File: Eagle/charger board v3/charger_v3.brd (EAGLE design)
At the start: 98.7 x 90.2 mm, 37 parts, among them IC1 IR2110D, Q2 IRFP240, Q3 MJE13003G

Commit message: benerin opto
benerin opto
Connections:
- removed net N$11: OK1.4, R1.2
- new net N$9: OK1.1, R1.2
- net 5V: now also OK1.4; no longer R1.1
- net PWM_SW1: now also R1.1; no longer OK1.1
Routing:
- net N$11: track 12.6 -> 0.00 mm
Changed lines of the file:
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@@
 <?xml version="1.0" encoding="utf-8"?>
 <!DOCTYPE eagle SYSTEM "eagle.dtd">
-<eagle version="9.6.1">
+<eagle version="9.6.2">
 <drawing>
 <settings>
-<setting alwaysvectorfont="yes"/>
+<setting alwaysvectorfont="no"/>
 <setting verticaltext="up"/>
 </settings>
@@
 <contactref element="ESP" pad="2"/>
 <contactref element="LM35" pad="3"/>
-<contactref element="R1" pad="1"/>
 <wire x1="93.98" y1="77.47" x2="93.98" y2="74.93" width="0.3048" layer="1"/>
 <wire x1="82.6008" y1="50.5968" x2="82.6008" y2="54.5592" width="0.3048" layer="16"/>
@@
 <wire x1="92.71" y1="33.02" x2="91.44" y2="33.02" width="0.3048" layer="16"/>
 <wire x1="91.44" y1="33.02" x2="89.5604" y2="34.8996" width="0.3048" layer="16"/>
-<wire x1="82.6008" y1="54.5592" x2="82.55" y2="54.61" width="0.3048" layer="16"/>
 <wire x1="97.282" y1="71.5772" x2="94.0308" y2="74.8284" width="0.3048" layer="16"/>
 <wire x1="97.282" y1="60.2996" x2="97.282" y2="71.5772" width="0.3048" layer="16"/>
@@
 <wire x1="82.6008" y1="54.7116" x2="83.6676" y2="55.7784" width="0.3048" layer="16"/>
 <wire x1="94.0308" y1="74.8284" x2="93.98" y2="74.93" width="0.3048" layer="16"/>
-<wire x1="82.6008" y1="54.7116" x2="82.55" y2="54.61" width="0.3048" layer="16"/>
 <wire x1="85.09" y1="77.47" x2="85.09" y2="78.74" width="0.3048" layer="1"/>
 <wire x1="85.09" y1="78.74" x2="86.36" y2="80.01" width="0.3048" layer="1"/>
@@
 <wire x1="91.44" y1="80.01" x2="93.98" y2="77.47" width="0.3048" layer="1"/>
 <contactref element="IC1" pad="9"/>
+<contactref element="OK1" pad="4"/>
+<wire x1="93.98" y1="74.93" x2="88.9" y2="71.12" width="0" layer="19" extent="1-1"/>
+<wire x1="82.6008" y1="54.5592" x2="82.6008" y2="54.7116" width="0" layer="19" extent="16-16"/>
 </signal>
 <signal name="VB">
@@
 <contactref element="ESP" pad="3"/>
 <contactref element="P_3V3" pad="1"/>
-<contactref element="OK1" pad="1"/>
 <wire x1="81.3816" y1="73.8124" x2="81.3816" y2="71.1708" width="0.3048" layer="16"/>
 <wire x1="82.55" y1="77.47" x2="82.55" y2="74.9808" width="0.3048" layer="16"/>
 <wire x1="82.55" y1="74.9808" x2="81.3816" y2="73.8124" width="0.3048" layer="16"/>
-<wire x1="81.3816" y1="71.1708" x2="81.28" y2="71.12" width="0.3048" layer="16"/>
 <wire x1="90.4748" y1="62.23" x2="92.71" y2="62.23" width="0.3048" layer="16"/>
 <wire x1="81.534" y1="71.1708" x2="90.4748" y2="62.23" width="0.3048" layer="16"/>
-<wire x1="81.534" y1="71.1708" x2="81.28" y2="71.12" width="0.3048" layer="16"/>
+<contactref element="R1" pad="1"/>
+<wire x1="81.534" y1="71.1708" x2="81.3816" y2="71.1708" width="0" layer="19" extent="16-16"/>
+<wire x1="82.55" y1="54.61" x2="92.71" y2="62.23" width="0" layer="19" extent="1-1"/>
 </signal>
 <signal name="PWM_SW2">
@@
 <contactref element="R9" pad="2"/>
 </signal>
-<signal name="N$11">
-<contactref element="OK1" pad="4"/>
+<signal name="N$9">
+<contactref element="OK1" pad="1"/>
 <contactref element="R1" pad="2"/>
-<wire x1="82.6008" y1="62.3316" x2="82.6008" y2="66.7258" width="0.3048" layer="1"/>
-<wire x1="86.995" y1="71.12" x2="88.9" y2="71.12" width="0.3048" layer="1"/>
-<wire x1="82.6008" y1="62.3316" x2="82.55" y2="62.23" width="0.3048" layer="1"/>
-<wire x1="82.6008" y1="66.7258" x2="86.995" y2="71.12" width="0.3048" layer="1"/>
+<wire x1="82.55" y1="62.23" x2="81.28" y2="71.12" width="0" layer="19" extent="1-1"/>
 </signal>
 </signals>

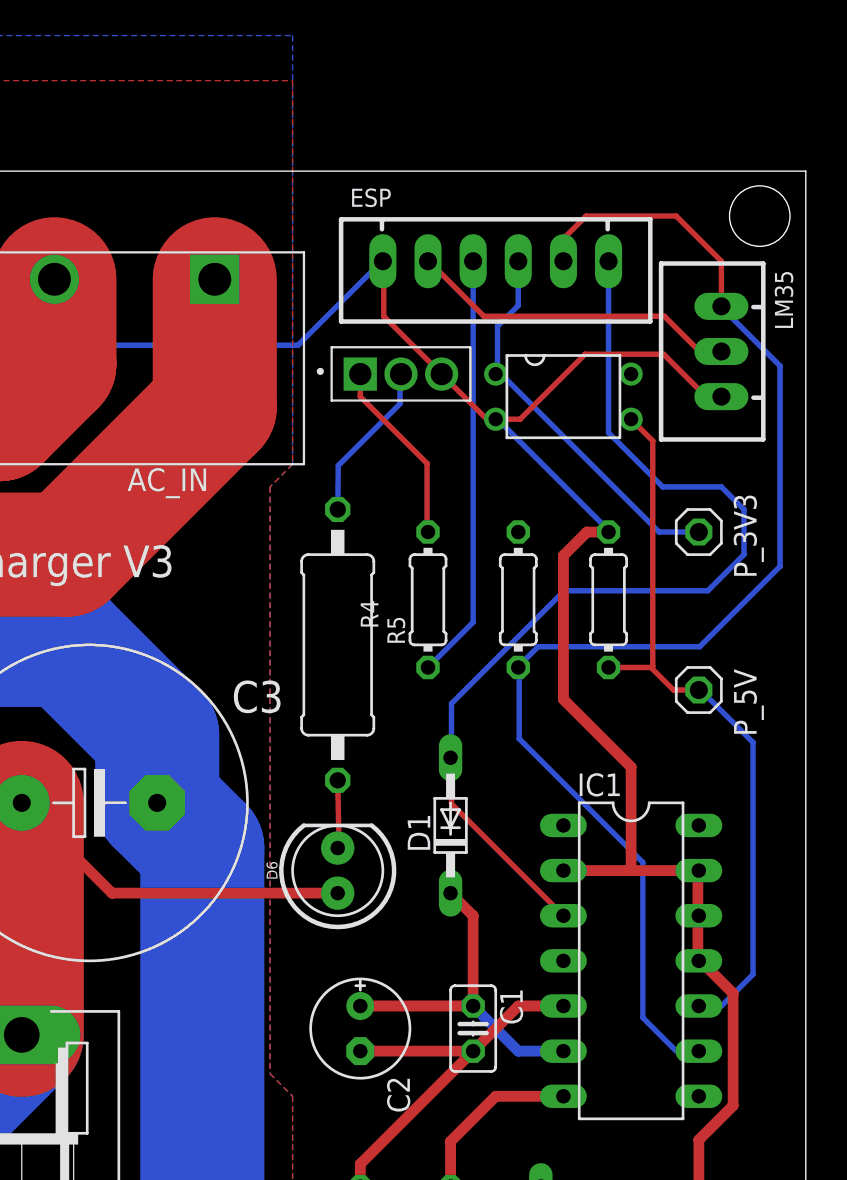
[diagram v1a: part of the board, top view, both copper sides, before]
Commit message: reroute opto
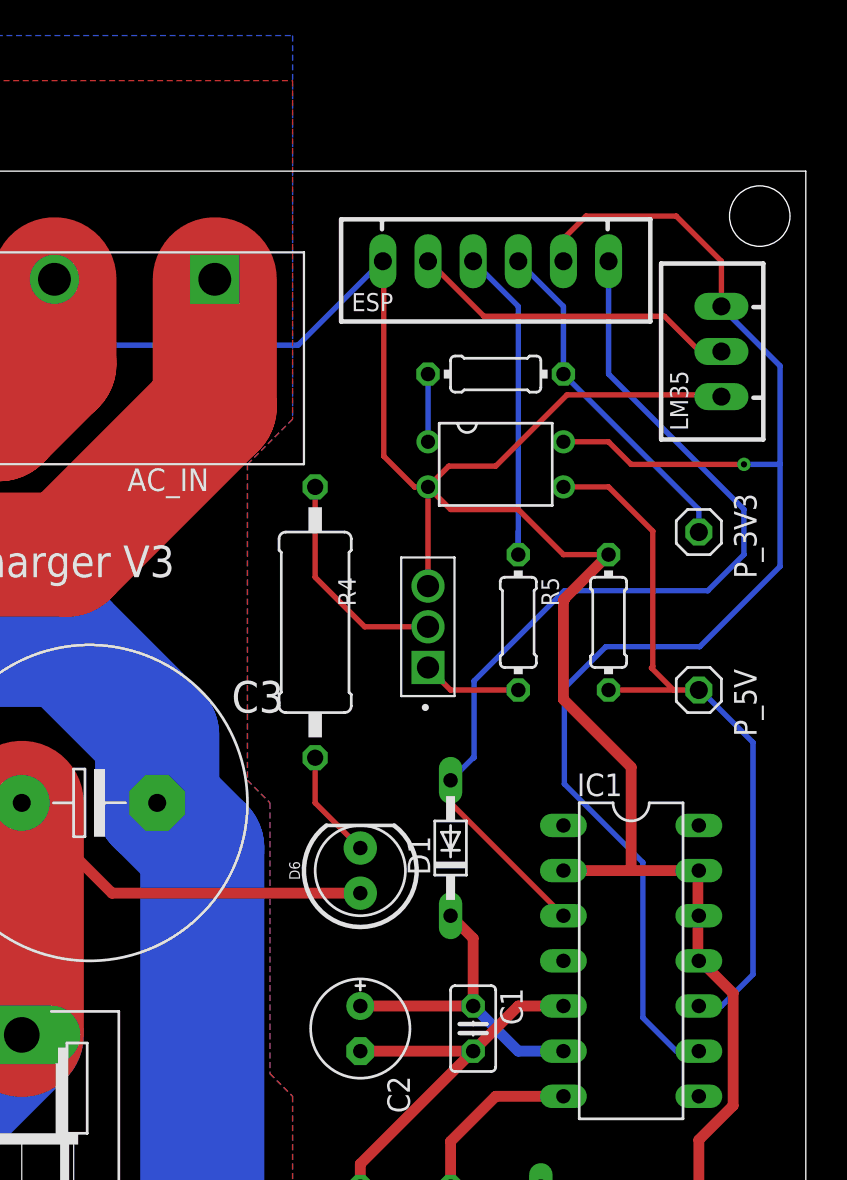
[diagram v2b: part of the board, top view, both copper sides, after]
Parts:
- moved Q3 16.9 mm to (77.5, 54.6), turned to 90 degrees
- moved R1 12.8 mm to (81.3, 71.1), turned to 180 degrees
- moved OK1 5.39 mm to (81.3, 66.0)
- moved R5 5.24 mm to (82.5, 57.1), turned to 270 degrees
- moved R4 1.80 mm to (71.1, 57.1)
- moved R7 1.27 mm to (87.6, 57.1)
- moved D1 1.27 mm to (78.7, 44.5)
- moved D6 1.27 mm to (73.7, 43.2)
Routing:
- net GND: track 345.4 -> 357.6 mm
- net 5V: track 73.7 -> 82.3 mm, vias 0 -> 1
- net PWM_SW2: track 23.9 -> 18.8 mm
- net N$5: track 10.5 -> 5.68 mm
- net N$9: track 0.00 -> 3.81 mm
- net N$3: track 9.07 -> 12.6 mm
- net N$4: track 3.89 -> 6.21 mm
- net PWM_SW1: track 21.7 -> 19.4 mm
- net 12V: track 56.2 -> 54.2 mm
- net V_OUT: track 69.1 -> 70.4 mm
- net VB: track 19.4 -> 18.1 mm

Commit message: update board chg v3
tambah probe buat D-S
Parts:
- added DRAIN, SOURCE: (no value), pinhead:1X01
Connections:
- net HVDC: now also DRAIN.1
- net NMOS_SOURCE: now also SOURCE.1
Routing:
- net HVDC: track 89.4 -> 100.6 mm
- net NMOS_SOURCE: track 177.8 -> 182.6 mm
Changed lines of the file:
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@@
 <drawing>
 <settings>
-<setting alwaysvectorfont="yes"/>
+<setting alwaysvectorfont="no"/>
 <setting verticaltext="up"/>
 </settings>
@@
 <attribute name="VALUE" x="87.1474" y="58.7756" size="0.9906" layer="27" ratio="10" rot="R270"/>
 </element>
+<element name="SOURCE" library="pinhead" library_urn="urn:adsk.eagle:library:325" package="1X01" package3d_urn="urn:adsk.eagle:package:22485/2" value="" x="6.35" y="34.29" smashed="yes">
+<attribute name="NAME" x="3.0988" y="35.6362" size="1.27" layer="25" ratio="10" rot="R270"/>
+<attribute name="POPULARITY" value="64" x="6.35" y="34.29" size="1.778" layer="27" display="off"/>
+<attribute name="VALUE" x="5.08" y="31.115" size="1.27" layer="27"/>
+</element>
+<element name="DRAIN" library="pinhead" library_urn="urn:adsk.eagle:library:325" package="1X01" package3d_urn="urn:adsk.eagle:package:22485/2" value="" x="8.89" y="77.47" smashed="yes">
+<attribute name="NAME" x="7.5438" y="79.2988" size="1.27" layer="25" ratio="10"/>
+<attribute name="POPULARITY" value="64" x="8.89" y="77.47" size="1.778" layer="27" display="off"/>
+<attribute name="VALUE" x="7.62" y="74.295" size="1.27" layer="27"/>
+</element>
 </elements>
 <signals>
@@
 <wire x1="50.8" y1="18.57375" x2="50.8" y2="21.59" width="0.6096" layer="16"/>
 <via x="50.8" y="21.59" extent="1-16" drill="0.35"/>
+<contactref element="SOURCE" pad="1"/>
+<wire x1="6.35" y1="34.29" x2="8.89" y2="31.75" width="0.3048" layer="16"/>
+<wire x1="8.89" y1="31.75" x2="8.89" y2="30.48" width="0.3048" layer="16"/>
 </signal>
 <signal name="PWM_12V" class="2">
@@
 <wire x1="8.73125" y1="49.37125" x2="8.73125" y2="46.99" width="0.3048" layer="1"/>
 <contactref element="Q2" pad="2"/>
+<contactref element="DRAIN" pad="1"/>
+<wire x1="8.89" y1="77.47" x2="17.13" y2="77.47" width="0.3048" layer="1"/>
+<wire x1="17.13" y1="77.47" x2="19.25" y2="75.35" width="0.3048" layer="1"/>
 </signal>
 <signal name="12V">

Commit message: update board chg v3
lebarin jalur, snubber
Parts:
- turned C5 to 180 degrees
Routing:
- net N$6: track 21.5 -> 15.3 mm
- net NMOS_SOURCE: track 182.6 -> 188.4 mm
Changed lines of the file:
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@@
 <attribute name="VALUE" x="71.49" y="80.22" size="1.27" layer="27" rot="R180"/>
 </element>
-<element name="C5" library="rcl" library_urn="urn:adsk.eagle:library:334" package="E7,5-18" package3d_urn="urn:adsk.eagle:package:23379/1" value="22uF" x="31.75" y="2.54" smashed="yes">
-<attribute name="NAME" x="39.751" y="7.62" size="1.778" layer="25" ratio="10"/>
-<attribute name="POPULARITY" value="6" x="31.75" y="2.54" size="1.778" layer="27" display="off"/>
-<attribute name="SPICEPREFIX" value="C" x="31.75" y="2.54" size="1.778" layer="27" display="off"/>
-<attribute name="VALUE" x="26.67" y="-1.7526" size="1.778" layer="27" ratio="10"/>
+<element name="C5" library="rcl" library_urn="urn:adsk.eagle:library:334" package="E7,5-18" package3d_urn="urn:adsk.eagle:package:23379/1" value="22uF" x="31.75" y="2.54" smashed="yes" rot="R180">
+<attribute name="NAME" x="23.749" y="-2.54" size="1.778" layer="25" ratio="10" rot="R180"/>
+<attribute name="POPULARITY" value="6" x="31.75" y="2.54" size="1.778" layer="27" rot="R180" display="off"/>
+<attribute name="SPICEPREFIX" value="C" x="31.75" y="2.54" size="1.778" layer="27" rot="R180" display="off"/>
+<attribute name="VALUE" x="36.83" y="6.8326" size="1.778" layer="27" ratio="10" rot="R180"/>
 </element>
 <element name="C6" library="rcl" library_urn="urn:adsk.eagle:library:334" package="E7,5-18" package3d_urn="urn:adsk.eagle:package:23379/1" value="22uF" x="12.7" y="2.54" smashed="yes" rot="R90">
@@
 <wire x1="80.01" y1="33.02" x2="73.66" y2="26.67" width="0.6096" layer="1"/>
 <wire x1="73.66" y1="26.67" x2="73.66" y2="25.4" width="0.6096" layer="1"/>
-<wire x1="8.89" y1="30.48" x2="25.833" y2="30.48" width="0.6096" layer="16"/>
-<wire x1="25.833" y1="30.48" x2="26.162" y2="30.151" width="0.6096" layer="16"/>
-<wire x1="45.0215" y1="3.2385" x2="36.2585" y2="3.2385" width="0.6096" layer="1"/>
-<wire x1="36.2585" y1="3.2385" x2="35.56" y2="2.54" width="0.6096" layer="1"/>
 <wire x1="11.684" y1="52.451" x2="14.859" y2="52.451" width="6.985" layer="16"/>
 <wire x1="26.162" y1="41.148" x2="14.859" y2="52.451" width="6.985" layer="16"/>
@@
 <wire x1="52.578" y1="-3.81" x2="52.578" y2="0.762" width="5.08" layer="1"/>
 <wire x1="52.578" y1="0.762" x2="52.07" y2="1.27" width="5.08" layer="1"/>
-<via x="46.19625" y="15.24" extent="1-16" drill="0.35"/>
+<via x="48.73625" y="7.62" extent="1-16" drill="0.35"/>
 <contactref element="R9" pad="1"/>
 <contactref element="C1" pad="2"/>
@@
 <contactref element="L1" pad="1"/>
 <contactref element="C2" pad="-"/>
-<wire x1="54.61" y1="25.4" x2="50.8" y2="21.59" width="0.6096" layer="1"/>
-<wire x1="73.66" y1="25.4" x2="54.61" y2="25.4" width="0.6096" layer="1"/>
-<wire x1="44.45" y1="8.41375" x2="42.148125" y2="6.111875" width="0.6096" layer="1"/>
-<wire x1="46.19625" y1="15.24" x2="44.45" y2="13.49375" width="0.6096" layer="1"/>
-<wire x1="44.45" y1="13.49375" x2="44.45" y2="8.41375" width="0.6096" layer="1"/>
-<wire x1="50.8" y1="18.57375" x2="47.46625" y2="15.24" width="0.6096" layer="16"/>
-<wire x1="46.19625" y1="15.24" x2="47.46625" y2="15.24" width="0.6096" layer="16"/>
-<wire x1="50.8" y1="18.57375" x2="50.8" y2="21.59" width="0.6096" layer="16"/>
-<via x="50.8" y="21.59" extent="1-16" drill="0.35"/>
+<wire x1="55.88" y1="25.4" x2="54.61" y2="24.13" width="0.6096" layer="1"/>
+<wire x1="73.66" y1="25.4" x2="55.88" y2="25.4" width="0.6096" layer="1"/>
+<wire x1="48.73625" y1="7.62" x2="43.65625" y2="7.62" width="0.6096" layer="1"/>
+<wire x1="43.65625" y1="7.62" x2="42.148125" y2="6.111875" width="0.6096" layer="1"/>
+<wire x1="54.61" y1="21.11375" x2="48.73625" y2="15.24" width="0.6096" layer="16"/>
+<wire x1="48.73625" y1="7.62" x2="48.73625" y2="15.24" width="0.6096" layer="16"/>
+<wire x1="54.61" y1="21.11375" x2="54.61" y2="24.13" width="0.6096" layer="16"/>
+<via x="54.61" y="24.13" extent="1-16" drill="0.35"/>
 <contactref element="SOURCE" pad="1"/>
 <wire x1="6.35" y1="34.29" x2="8.89" y2="31.75" width="0.3048" layer="16"/>
 <wire x1="8.89" y1="31.75" x2="8.89" y2="30.48" width="0.3048" layer="16"/>
+<wire x1="8.89" y1="30.48" x2="25.833" y2="30.48" width="6.985" layer="16"/>
+<wire x1="25.833" y1="30.48" x2="26.162" y2="30.151" width="6.985" layer="16"/>
+<wire x1="27.94" y1="2.54" x2="27.94" y2="7.62" width="6.985" layer="1"/>
+<wire x1="27.94" y1="7.62" x2="34.29" y2="13.97" width="6.985" layer="1"/>
 </signal>
 <signal name="PWM_12V" class="2">
@@
 <signal name="N$6">
 <contactref element="R8" pad="1"/>
-<wire x1="41.91" y1="15.24" x2="36.83" y2="15.24" width="0.6096" layer="16"/>
-<wire x1="36.83" y1="15.24" x2="27.94" y2="6.35" width="0.6096" layer="16"/>
-<wire x1="27.94" y1="6.35" x2="27.94" y2="2.54" width="0.6096" layer="16"/>
 <contactref element="C5" pad="+"/>
+<wire x1="41.91" y1="15.24" x2="41.91" y2="8.89" width="6.985" layer="16"/>
+<wire x1="41.91" y1="8.89" x2="35.56" y2="2.54" width="6.985" layer="16"/>
 </signal>
 <signal name="N$7">
 <contactref element="C6" pad="-"/>
-<wire x1="12.7" y1="6.35" x2="8.89" y2="10.16" width="0.6096" layer="16"/>
-<wire x1="8.89" y1="10.16" x2="8.89" y2="15.24" width="0.6096" layer="16"/>
 <contactref element="R9" pad="2"/>
+<wire x1="12.7" y1="6.35" x2="8.89" y2="10.16" width="6.985" layer="16"/>
+<wire x1="8.89" y1="10.16" x2="8.89" y2="15.24" width="6.985" layer="16"/>
 </signal>
 <signal name="N$9">
